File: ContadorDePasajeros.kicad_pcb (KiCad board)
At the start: 2 copper layers, 56.2 x 25.8 mm, 13 parts, among them J1 Conector_in, J3 Conector_esp, U1 ESP01

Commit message: Serigrafia, agujeros y ajustes
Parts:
- added MH1: MountingHole, Mounting_Holes:MountingHole_2.5mm, F.Cu at (27.5, 27.2)
- added MH2: MountingHole, Mounting_Holes:MountingHole_2.5mm, F.Cu at (77.0, 27.5)
- added MH3: MountingHole, Mounting_Holes:MountingHole_2.5mm, F.Cu at (27.2, 48.5)
- added MH4: MountingHole, Mounting_Holes:MountingHole_2.5mm, F.Cu at (77.0, 48.5)
- moved U1 0.25 mm to (56.5, 34.5)
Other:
- board size 56.2 x 25.8 mm -> 56.2 x 27.8 mm
- board text added: "Contador de pasajeros v1.0"
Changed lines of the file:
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@@
   (general
     (thickness 1.6)
-    (drawings 4)
+    (drawings 5)
     (tracks 109)
     (zones 0)
-    (modules 13)
+    (modules 17)
     (nets 11)
   )
@@
     (0 F.Cu signal hide)
     (31 B.Cu signal hide)
-    (32 B.Adhes user hide)
+    (32 B.Adhes user)
     (33 F.Adhes user)
-    (34 B.Paste user hide)
+    (34 B.Paste user)
     (35 F.Paste user)
-    (36 B.SilkS user hide)
+    (36 B.SilkS user)
     (37 F.SilkS user)
-    (38 B.Mask user hide)
+    (38 B.Mask user)
     (39 F.Mask user)
     (40 Dwgs.User user)
@@
   )
   (module ESP8266:ESP-01 (layer F.Cu)
-    (at 56.75 34.5)
+    (at 56.5 34.5)
     (descr "Module, ESP-8266, ESP-01, 8 pin")
     (tags "Module ESP-8266 ESP8266")
@@
     )
   )
-  (gr_line (start 24 26) (end 80.25 26) (layer Edge.Cuts) (width 0.15))
-  (gr_line (start 80.25 51.75) (end 80.25 26) (layer Edge.Cuts) (width 0.15))
-  (gr_line (start 24 51.75) (end 24 26) (layer Edge.Cuts) (width 0.15))
+  (module Mounting_Holes:MountingHole_2.5mm (layer F.Cu)
+    (at 27.5 27.25)
+    (descr "Mounting Hole 2.5mm, no annular")
+    (tags "mounting hole 2.5mm no annular")
+    (attr virtual)
+    (fp_text reference MH1 (at 3.5 0) (layer F.SilkS)
+      (effects (font (size 1 1) (thickness 0.15)))
+    )
+    (fp_text value MountingHole (at 1.75 -1.75) (layer F.Fab)
+      (effects (font (size 1 1) (thickness 0.15)))
+    )
+    (fp_text user %R (at 3.5 0) (layer F.Fab)
+      (effects (font (size 1 1) (thickness 0.15)))
+    )
+    (fp_circle (center 0 0) (end 2.5 0) (layer Cmts.User) (width 0.15))
+    (fp_circle (center 0 0) (end 2.75 0) (layer F.CrtYd) (width 0.05))
+    (pad 1 np_thru_hole circle (at 0 0) (size 2.5 2.5) (drill 2.5) (layers *.Cu *.Mask))
+  )
+  (module Mounting_Holes:MountingHole_2.5mm (layer F.Cu)
+    (at 77 27.5)
+    (descr "Mounting Hole 2.5mm, no annular")
+    (tags "mounting hole 2.5mm no annular")
+    (attr virtual)
+    (fp_text reference MH2 (at -3.75 0) (layer F.SilkS)
+      (effects (font (size 1 1) (thickness 0.15)))
+    )
+    (fp_text value MountingHole (at -2.25 -2) (layer F.Fab)
+      (effects (font (size 1 1) (thickness 0.15)))
+    )
+    (fp_circle (center 0 0) (end 2.75 0) (layer F.CrtYd) (width 0.05))
+    (fp_circle (center 0 0) (end 2.5 0) (layer Cmts.User) (width 0.15))
+    (fp_text user %R (at -3.75 0) (layer F.Fab)
+      (effects (font (size 1 1) (thickness 0.15)))
+    )
+    (pad 1 np_thru_hole circle (at 0 0) (size 2.5 2.5) (drill 2.5) (layers *.Cu *.Mask))
+  )
+  (module Mounting_Holes:MountingHole_2.5mm (layer F.Cu)
+    (at 27.25 48.5)
+    (descr "Mounting Hole 2.5mm, no annular")
+    (tags "mounting hole 2.5mm no annular")
+    (attr virtual)
+    (fp_text reference MH3 (at 3.75 0) (layer F.SilkS)
+      (effects (font (size 1 1) (thickness 0.15)))
+    )
+    (fp_text value MountingHole (at 2 2) (layer F.Fab)
+      (effects (font (size 1 1) (thickness 0.15)))
+    )
+    (fp_text user %R (at 3.75 0) (layer F.Fab)
+      (effects (font (size 1 1) (thickness 0.15)))
+    )
+    (fp_circle (center 0 0) (end 2.5 0) (layer Cmts.User) (width 0.15))
+    (fp_circle (center 0 0) (end 2.75 0) (layer F.CrtYd) (width 0.05))
+    (pad 1 np_thru_hole circle (at 0 0) (size 2.5 2.5) (drill 2.5) (layers *.Cu *.Mask))
+  )
+  (module Mounting_Holes:MountingHole_2.5mm (layer F.Cu)
+    (at 77 48.5)
+    (descr "Mounting Hole 2.5mm, no annular")
+    (tags "mounting hole 2.5mm no annular")
+    (attr virtual)
+    (fp_text reference MH4 (at -3.75 0.25) (layer F.SilkS)
+      (effects (font (size 1 1) (thickness 0.15)))
+    )
+    (fp_text value MountingHole (at -2 2.25) (layer F.Fab)
+      (effects (font (size 1 1) (thickness 0.15)))
+    )
+    (fp_circle (center 0 0) (end 2.75 0) (layer F.CrtYd) (width 0.05))
+    (fp_circle (center 0 0) (end 2.5 0) (layer Cmts.User) (width 0.15))
+    (fp_text user %R (at -3.75 0.25) (layer F.Fab)
+      (effects (font (size 1 1) (thickness 0.15)))
+    )
+    (pad 1 np_thru_hole circle (at 0 0) (size 2.5 2.5) (drill 2.5) (layers *.Cu *.Mask))
+  )
+  (gr_text "Contador de pasajeros v1.0" (at 58.25 50) (layer F.SilkS)
+    (effects (font (size 1 1) (thickness 0.25)))
+  )
+  (gr_line (start 24 24) (end 80.25 24) (layer Edge.Cuts) (width 0.15))
+  (gr_line (start 80.25 51.75) (end 80.25 24) (layer Edge.Cuts) (width 0.15))
+  (gr_line (start 24 51.75) (end 24 24) (layer Edge.Cuts) (width 0.15))
   (gr_line (start 80.25 51.75) (end 24 51.75) (layer Edge.Cuts) (width 0.15))
   (segment (start 30.62 42.12) (end 30 41.5) (width 0.25) (layer B.Cu) (net 1))
@@
     )
   )
+  (zone (net 1) (net_name GNA) (layer B.Cu) (hatch edge 0.508)
+    (connect_pads (clearance 0.508))
+    (min_thickness 0.254)
+    (fill yes (arc_segments 16) (thermal_gap 0.508) (thermal_bridge_width 0.508))
+    (polygon
+      (pts
+        (xy 24.25 51.5) (xy 79.75 51.5) (xy 79.75 24.5) (xy 24.25 24.25)
+      )
+    )
+  )
   (zone (net 1) (net_name GNA) (layer F.Cu) (hatch edge 0.508)
     (connect_pads (clearance 0.508))
@@
     (polygon
       (pts
-        (xy 24.25 26.25) (xy 24.25 51.5) (xy 79.75 51.5) (xy 79.75 26.5)
+        (xy 79.75 24.5) (xy 79.75 51.5) (xy 24.25 51.5) (xy 24.5 24.25)
       )
     )
-  )
-  (zone (net 1) (net_name GNA) (layer B.Cu) (hatch edge 0.508)
-    (connect_pads (clearance 0.508))
-    (min_thickness 0.254)
-    (fill yes (arc_segments 16) (thermal_gap 0.508) (thermal_bridge_width 0.508))
-    (polygon
-      (pts
-        (xy 24.25 51.5) (xy 79.75 51.5) (xy 79.75 26.5) (xy 24.25 26.25)
-      )
-    )

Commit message: Correcciones adrian
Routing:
- net VCA: track 40.8 -> 44.5 mm
- net GNA: track 52.5 -> 53.4 mm
- net RSA: track 26.1 -> 26.9 mm
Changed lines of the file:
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@@
     (thickness 1.6)
     (drawings 5)
-    (tracks 109)
+    (tracks 116)
     (zones 0)
     (modules 17)
@@
     (descr "Module, ESP-8266, ESP-01, 8 pin")
     (tags "Module ESP-8266 ESP8266")
-    (fp_text reference U1 (at 0.254 -4.572) (layer F.SilkS)
+    (fp_text reference U1 (at 1.5 12.25) (layer F.SilkS)
       (effects (font (size 1 1) (thickness 0.15)))
     )
@@
     (descr "Through hole straight socket strip, 2x04, 2.54mm pitch, double cols (from Kicad 4.0.7), script generated")
     (tags "Through hole socket strip THT 2x04 2.54mm double row")
-    (fp_text reference J3 (at 3.25 3.75) (layer F.SilkS)
+    (fp_text reference J3 (at -1.25 -4.5) (layer F.SilkS)
       (effects (font (size 1 1) (thickness 0.15)))
     )
@@
     (tags "mounting hole 2.5mm no annular")
     (attr virtual)
-    (fp_text reference MH1 (at 3.5 0) (layer F.SilkS)
-      (effects (font (size 1 1) (thickness 0.15)))
-    )
-    (fp_text value MountingHole (at 1.75 -1.75) (layer F.Fab)
+    (fp_text reference MH1 (at 3.5 0) (layer F.SilkS) hide
+      (effects (font (size 1 1) (thickness 0.15)))
+    )
+    (fp_text value MountingHole (at 1.75 -1.75) (layer F.Fab) hide
       (effects (font (size 1 1) (thickness 0.15)))
     )
@@
     (tags "mounting hole 2.5mm no annular")
     (attr virtual)
-    (fp_text reference MH2 (at -3.75 0) (layer F.SilkS)
+    (fp_text reference MH2 (at -3.75 0) (layer F.SilkS) hide
       (effects (font (size 1 1) (thickness 0.15)))
     )
@@
     (tags "mounting hole 2.5mm no annular")
     (attr virtual)
-    (fp_text reference MH3 (at 3.75 0) (layer F.SilkS)
-      (effects (font (size 1 1) (thickness 0.15)))
-    )
-    (fp_text value MountingHole (at 2 2) (layer F.Fab)
+    (fp_text reference MH3 (at 3.75 0) (layer F.SilkS) hide
+      (effects (font (size 1 1) (thickness 0.15)))
+    )
+    (fp_text value MountingHole (at 2 2) (layer F.Fab) hide
       (effects (font (size 1 1) (thickness 0.15)))
     )
@@
     (tags "mounting hole 2.5mm no annular")
     (attr virtual)
-    (fp_text reference MH4 (at -3.75 0.25) (layer F.SilkS)
+    (fp_text reference MH4 (at -3.75 0.25) (layer F.SilkS) hide
       (effects (font (size 1 1) (thickness 0.15)))
     )
@@
   (segment (start 48.475 31.075) (end 47.4 30) (width 0.25) (layer F.Cu) (net 1))
   (segment (start 48.475 38.225) (end 48.45 38.25) (width 0.25) (layer F.Cu) (net 1))
-  (segment (start 48.475 34.5) (end 48.475 38.225) (width 0.25) (layer F.Cu) (net 1))
   (segment (start 59 33.4) (end 57.6 32) (width 0.25) (layer F.Cu) (net 1))
   (segment (start 59 34.5) (end 59 33.4) (width 0.25) (layer F.Cu) (net 1))
@@
   (segment (start 37.322081 40.5) (end 44.25 40.5) (width 0.25) (layer B.Cu) (net 1))
   (segment (start 44.25 40.5) (end 46.25 38.5) (width 0.25) (layer B.Cu) (net 1))
-  (segment (start 48.2 38.5) (end 48.45 38.25) (width 0.25) (layer F.Cu) (net 1))
-  (segment (start 46.25 38.5) (end 48.2 38.5) (width 0.25) (layer F.Cu) (net 1))
+  (segment (start 48.475 36.75) (end 47.75 36.75) (width 0.25) (layer F.Cu) (net 1))
+  (segment (start 48.475 34.5) (end 48.475 36.75) (width 0.25) (layer F.Cu) (net 1))
+  (segment (start 46.25 38.5) (end 47 38.5) (width 0.25) (layer F.Cu) (net 1))
+  (segment (start 47.25 38.25) (end 48.45 38.25) (width 0.25) (layer F.Cu) (net 1))
+  (segment (start 47 38.5) (end 47.25 38.25) (width 0.25) (layer F.Cu) (net 1))
+  (segment (start 47.25 38.25) (end 47.25 37.25) (width 0.25) (layer F.Cu) (net 1))
+  (segment (start 47.75 36.75) (end 47.25 37.25) (width 0.25) (layer F.Cu) (net 1))
   (segment (start 34.5 37.04) (end 37.46 37.04) (width 0.25) (layer B.Cu) (net 2))
   (segment (start 37.46 37.04) (end 38.25 36.25) (width 0.25) (layer B.Cu) (net 2))
@@
   (segment (start 55.257919 39.58) (end 56.46 39.58) (width 0.25) (layer F.Cu) (net 3))
   (segment (start 54.587919 40.25) (end 55.257919 39.58) (width 0.25) (layer F.Cu) (net 3))
-  (segment (start 42.05 41.75) (end 43.55 40.25) (width 0.25) (layer F.Cu) (net 3))
   (segment (start 44.5 40.25) (end 44.5 33) (width 0.25) (layer F.Cu) (net 3))
   (segment (start 44.5 40.25) (end 54.587919 40.25) (width 0.25) (layer F.Cu) (net 3))
-  (segment (start 43.55 40.25) (end 44.5 40.25) (width 0.25) (layer F.Cu) (net 3))
   (segment (start 43.3 31.8) (end 43.3 30) (width 0.25) (layer F.Cu) (net 3))
   (segment (start 44.5 33) (end 43.3 31.8) (width 0.25) (layer F.Cu) (net 3))
+  (segment (start 42.05 41.75) (end 44.5 41.75) (width 0.25) (layer F.Cu) (net 3))
+  (segment (start 44.5 41.75) (end 44.5 40.25) (width 0.25) (layer F.Cu) (net 3))
   (segment (start 55.257919 37.04) (end 55.047919 37.25) (width 0.25) (layer B.Cu) (net 4))
   (segment (start 56.46 37.04) (end 55.257919 37.04) (width 0.25) (layer B.Cu) (net 4))
@@
   (segment (start 42 34.5) (end 43.5 34.5) (width 0.25) (layer F.Cu) (net 6))
   (segment (start 45.5 34.5) (end 47 33) (width 0.25) (layer B.Cu) (net 6))
-  (segment (start 45.5 34.5) (end 45.75 34.5) (width 0.25) (layer B.Cu) (net 6))
   (segment (start 43.5 34.5) (end 45.5 34.5) (width 0.25) (layer B.Cu) (net 6))
   (segment (start 47 33) (end 51 33) (width 0.25) (layer B.Cu) (net 6))
@@
   (segment (start 30 35.5) (end 31 34.5) (width 0.25) (layer B.Cu) (net 8))
   (segment (start 30 40) (end 30 35.5) (width 0.25) (layer B.Cu) (net 8))
-  (segment (start 35.83 38.25) (end 34.5 39.58) (width 0.25) (layer F.Cu) (net 8))
-  (segment (start 39.95 38.25) (end 35.83 38.25) (width 0.25) (layer F.Cu) (net 8))
   (segment (start 40 38.3) (end 39.95 38.25) (width 0.25) (layer F.Cu) (net 8))
   (segment (start 40 41.75) (end 40 38.3) (width 0.25) (layer F.Cu) (net 8))
-  (segment (start 47.2 43.5) (end 48.45 42.25) (width 0.25) (layer F.Cu) (net 8))
-  (segment (start 40.95 43.5) (end 47.2 43.5) (width 0.25) (layer F.Cu) (net 8))
   (segment (start 40 41.75) (end 40 42.55) (width 0.25) (layer F.Cu) (net 8))
-  (segment (start 40 42.55) (end 40.95 43.5) (width 0.25) (layer F.Cu) (net 8))
   (segment (start 55.257919 42.12) (end 53.127919 44.25) (width 0.25) (layer B.Cu) (net 8))
   (segment (start 56.46 42.12) (end 55.257919 42.12) (width 0.25) (layer B.Cu) (net 8))
@@
   (segment (start 53.127919 44.25) (end 49 44.25) (width 0.25) (layer B.Cu) (net 8))
   (segment (start 49 44.25) (end 48.75 44) (width 0.25) (layer B.Cu) (net 8))
-  (segment (start 48.75 42.55) (end 48.45 42.25) (width 0.25) (layer F.Cu) (net 8))
-  (segment (start 48.75 44) (end 48.75 42.55) (width 0.25) (layer F.Cu) (net 8))
+  (segment (start 40 43.5) (end 40 42.55) (width 0.25) (layer F.Cu) (net 8))
+  (segment (start 38.25 43.5) (end 40 43.5) (width 0.25) (layer F.Cu) (net 8))
+  (segment (start 37.5 42.75) (end 38.25 43.5) (width 0.25) (layer F.Cu) (net 8))
+  (segment (start 37.5 40.25) (end 37.5 42.75) (width 0.25) (layer F.Cu) (net 8))
+  (segment (start 36.83 39.58) (end 37.5 40.25) (width 0.25) (layer F.Cu) (net 8))
+  (segment (start 34.5 39.58) (end 36.83 39.58) (width 0.25) (layer F.Cu) (net 8))
+  (segment (start 48.75 43) (end 48.75 44) (width 0.25) (layer F.Cu) (net 8))
+  (segment (start 48.25 43.5) (end 48.75 43) (width 0.25) (layer F.Cu) (net 8))
+  (segment (start 40 43.5) (end 48.25 43.5) (width 0.25) (layer F.Cu) (net 8))
+  (segment (start 48.475 42.725) (end 48.475 41.75) (width 0.25) (layer F.Cu) (net 8))
+  (segment (start 48.75 43) (end 48.475 42.725) (width 0.25) (layer F.Cu) (net 8))
   (via (at 53.5 33.25) (size 1) (drill 0.5) (layers F.Cu B.Cu) (net 9))
   (segment (start 53.475001 33.274999) (end 53.5 33.25) (width 0.25) (layer F.Cu) (net 9))

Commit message: Correcciones Adrian
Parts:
- moved MH2 1.35 mm to (75.8, 28.0)
- moved MH3 1.35 mm to (28.5, 48.0)
- moved MH4 1.00 mm to (76.0, 48.5)
- moved MH1 0.90 mm to (28.2, 27.8)
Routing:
- net Net-(Flash1-Pad2): track 47.0 -> 50.2 mm
- net RSA: track 26.9 -> 29.6 mm
- net VCA: track 44.5 -> 47.0 mm
- net GNA: track 53.4 -> 55.6 mm
- net G0A: track 25.6 -> 27.4 mm
- net RXA: track 30.2 -> 30.9 mm
- added copper zone on B.Cu, net VCA
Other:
- board text added: "Margen: 0.25 mm Ancho pista: 0.25 mm Diametro Via: 1 mm Taladro via: 0.4 mm Cuadricula: 0.25 mm Fabricante: https://www.pcbcart.com/pcb-fab/hdi-pcb.html"

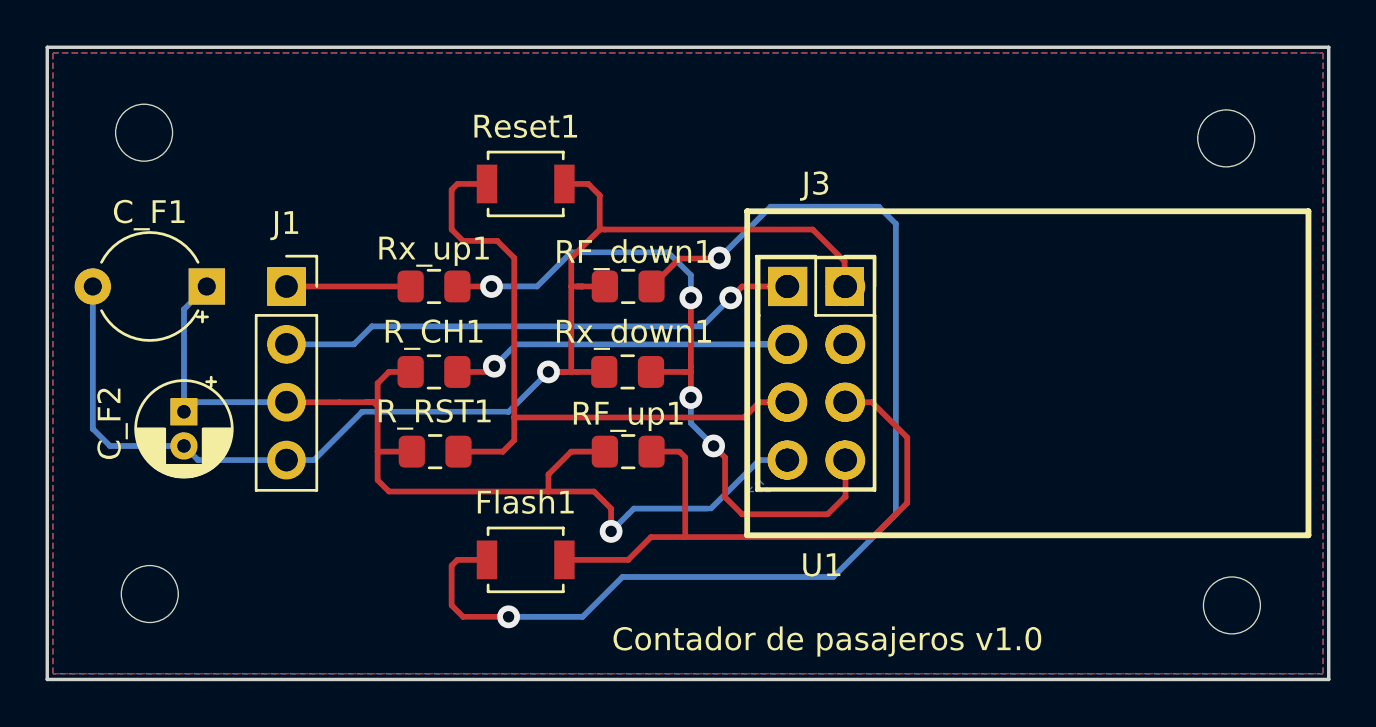
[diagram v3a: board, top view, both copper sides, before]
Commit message: Ajuste de ancho de pistas
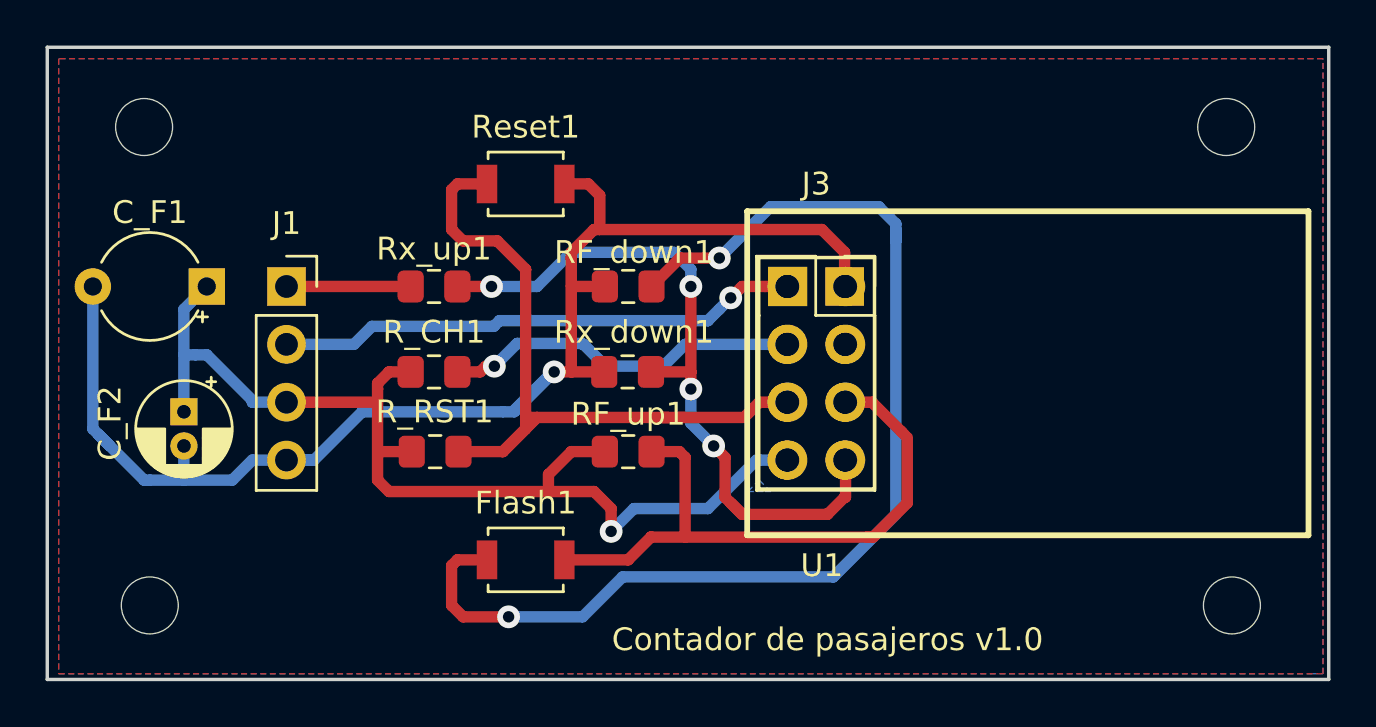
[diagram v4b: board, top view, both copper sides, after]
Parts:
- moved MH2 0.50 mm to (75.8, 27.5)
- moved MH3 0.50 mm to (28.5, 48.5)
- moved MH1 0.25 mm to (28.2, 27.5)
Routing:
- net VCA: track 47.0 -> 67.8 mm
- net GNA: track 55.6 -> 65.8 mm
- net G0A: track 27.4 -> 36.9 mm
- net RSA: track 29.6 -> 37.4 mm
- net Net-(Flash1-Pad2): track 50.2 -> 55.7 mm
- net RXA: track 30.9 -> 33.9 mm
- net TXA: track 23.0 -> 24.0 mm
- net CHA: track 16.2 -> 17.0 mm
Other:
- net class Default: clearance 0.25 -> 0.5; trace_width 0.25 -> 0.5
- rule trace_clearance: 0.25 -> 0.5
- board text added: "Margen: 0.5 mm Ancho pista: 0.5 mm Diametro Via: 1 mm Taladro via: 0.4 mm Cuadricula: 0.5 mm Fabricante: https://www.pcbcart.com/pcb-fab/hdi-pcb.html"
- board text removed: "Margen: 0.25 mm Ancho pista: 0.25 mm Diametro Via: 1 mm Taladro via: 0.4 mm Cuadricula: 0.25 mm Fabricante: https://www.pcbcart.com/pcb-fab/hdi-pcb.html"
